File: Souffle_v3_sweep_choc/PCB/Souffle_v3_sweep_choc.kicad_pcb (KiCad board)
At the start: 2 copper layers, 132.1 x 108 mm, 84 parts, among them J1 LED, J2 4PIN, J3 OLED, J4 Conn_01x01_Female, J5 Conn_01x01_Female, SW1 SW_PUSH, SW10 SW_PUSH, SW11 SW_PUSH, SW12 SW_PUSH, SW13 SW_PUSH, SW14 SW_PUSH, SW15 SW_PUSH, SW16 SW_PUSH, SW17 SW_PUSH, SW18 SW_PUSH, SW19 SW_PUSH, SW2 SW_PUSH, SW20 SW_PUSH, SW21 SW_PUSH, SW22 SW_PUSH, SW23 SW_PUSH, SW24 SW_PUSH, SW25 SW_PUSH, SW25b1 RotaryEncoder_Switch, SW26 SW_PUSH, SW27 SW_PUSH, SW28 SW_PUSH, SW29 SW_PUSH, SW3 SW_PUSH, SW30 SW_PUSH, SW31 SW_SPDT, SW4 SW_PUSH, SW5 SW_PUSH, SW6 SW_PUSH, SW7 SW_PUSH, SW8 SW_PUSH, SW9 SW_PUSH, U1 ProMicro

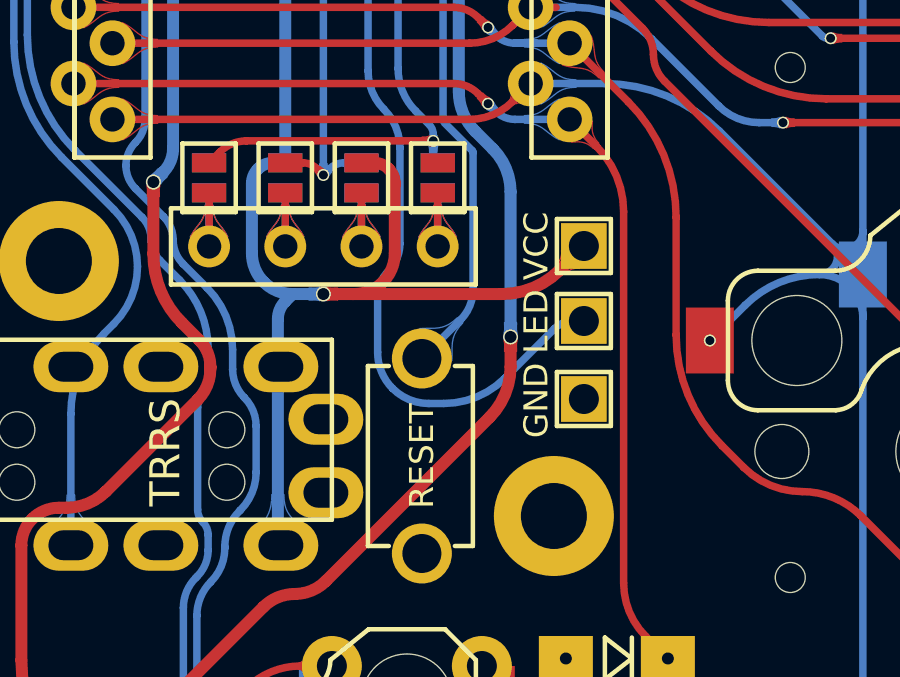
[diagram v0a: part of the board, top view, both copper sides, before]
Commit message: Fixed small bug, completed comment layer.
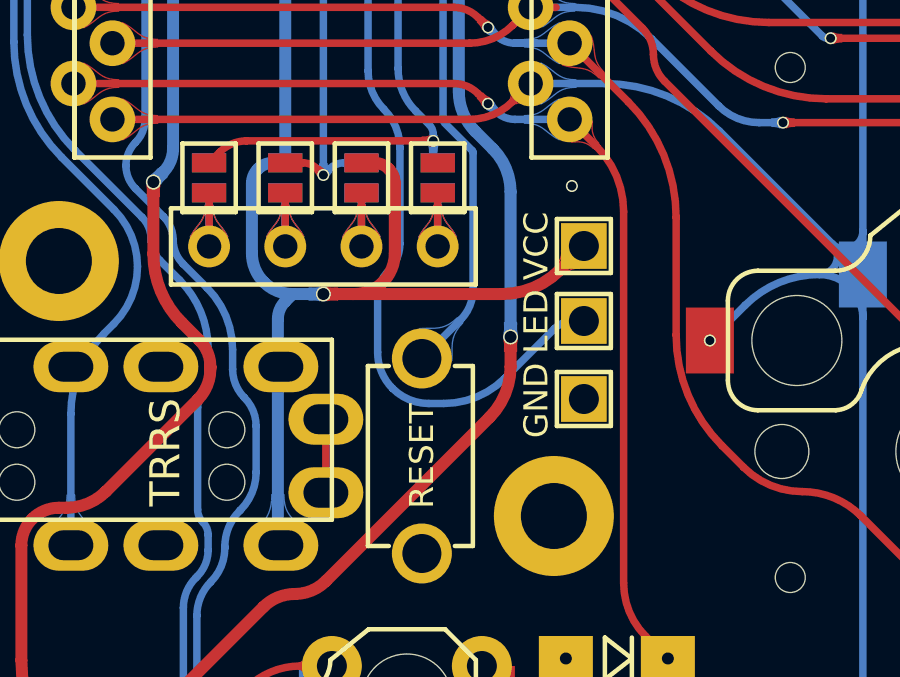
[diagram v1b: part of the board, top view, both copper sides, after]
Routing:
- net unconnected-(J2-Pad4): track 0.00 -> 2.45 mm
- net GND: vias 0 -> 1

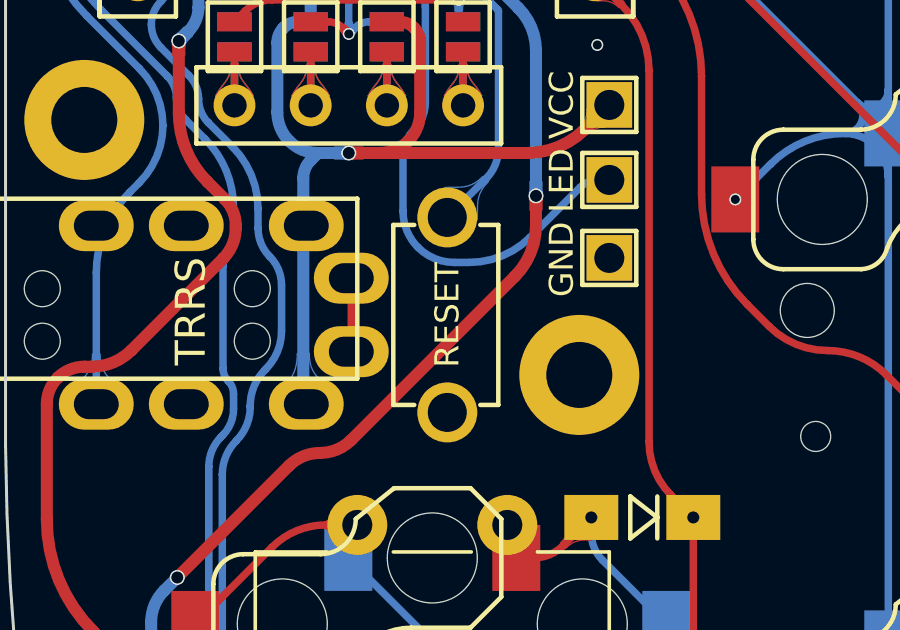
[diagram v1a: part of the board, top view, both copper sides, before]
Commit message: Push reset button away from the TRRS conenctor.
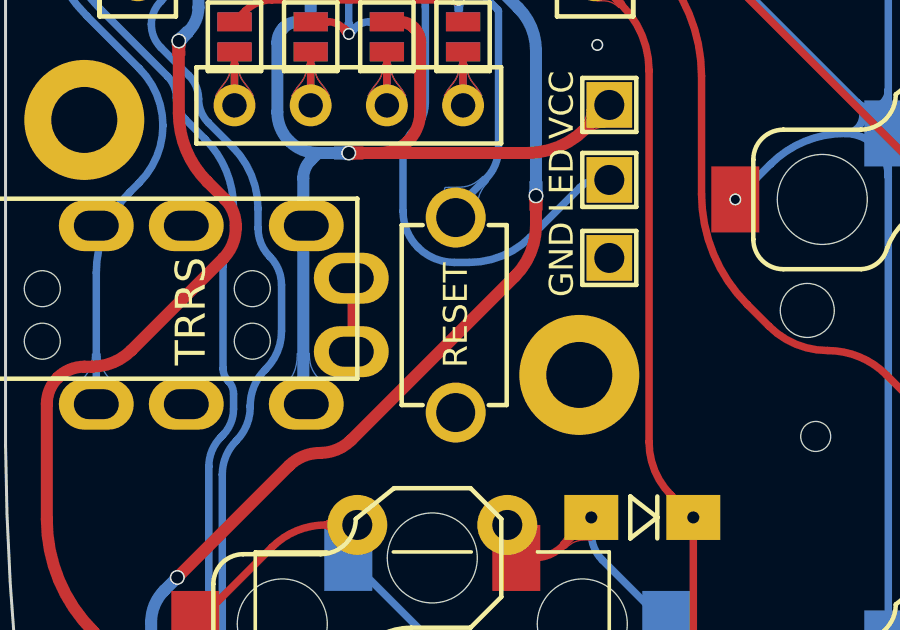
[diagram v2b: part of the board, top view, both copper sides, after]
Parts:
- moved RSW1 0.28 mm to (88.9, 85.7)
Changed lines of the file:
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@@
   )
   (footprint "SofleKeyboard-footprint:TACT_SWITCH_TVBP06" (layer "F.Cu")
-    (at 88.634 85.723139 90)
+    (at 88.914548 85.727296 90)
     (property "Sheetfile" "Souffle_v3_sweep.kicad_sch")
     (property "Sheetname" "")

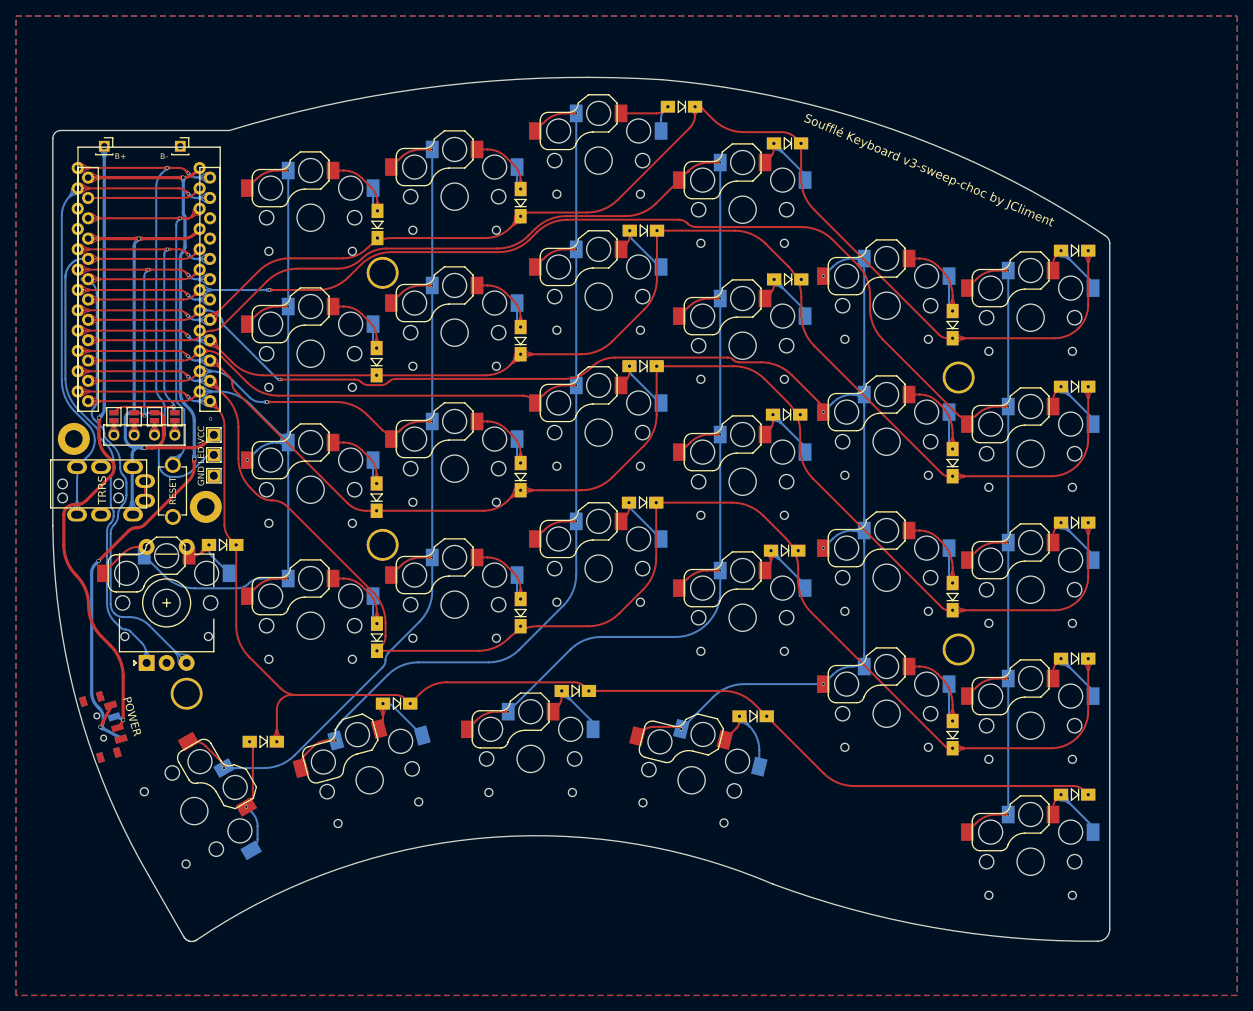
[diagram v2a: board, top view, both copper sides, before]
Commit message: Small changes to make sure the components do not touch each other or the board.
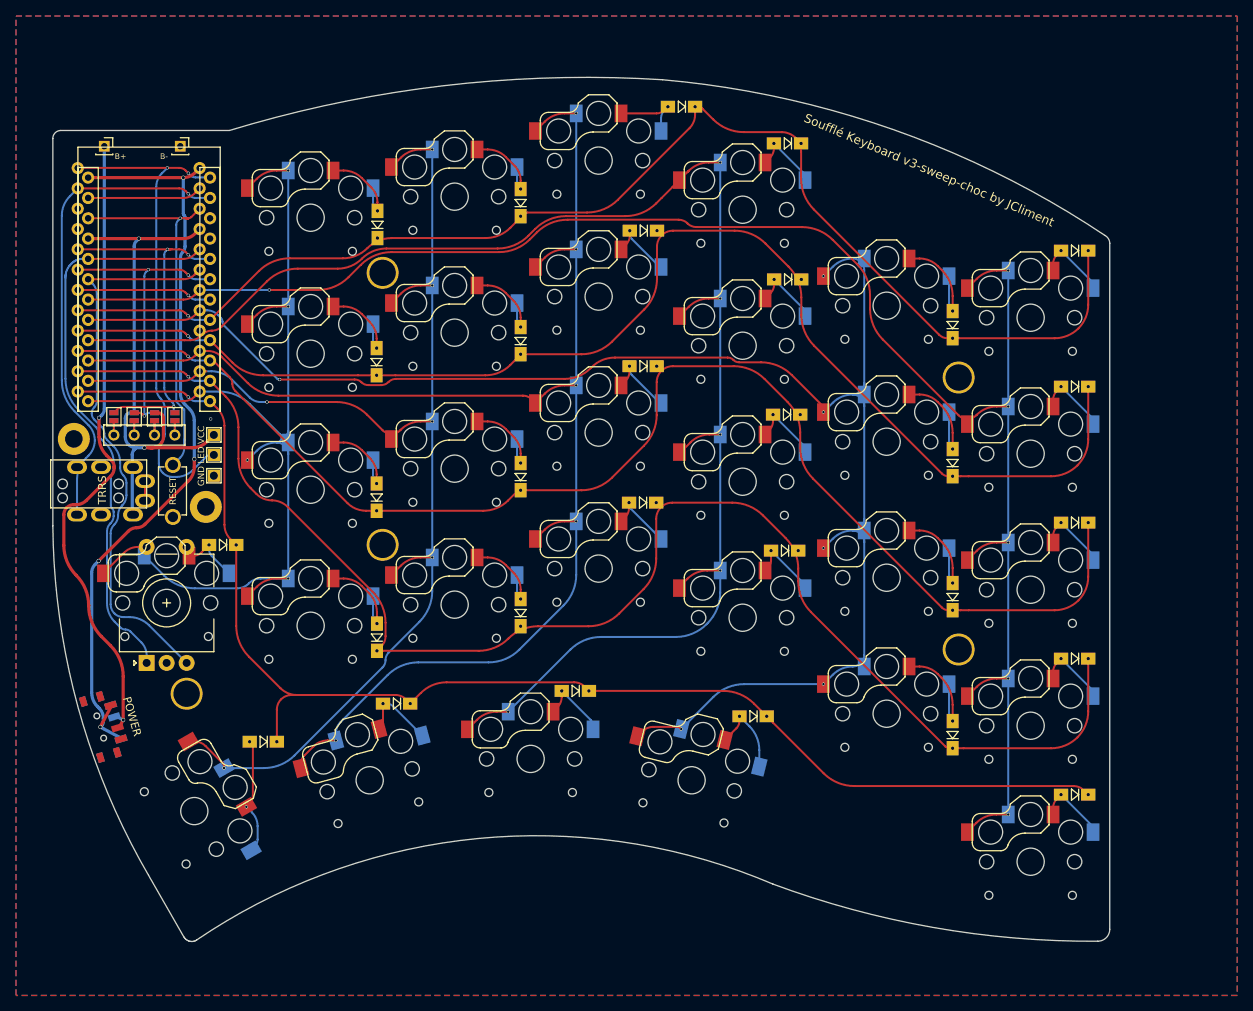
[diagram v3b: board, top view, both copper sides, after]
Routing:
- net row2: track 171.1 -> 170.1 mm
- net row3: track 185.9 -> 185.0 mm
- net row1: track 164.8 -> 163.9 mm
- net row4: track 172.3 -> 173.1 mm
- net RESET: track 46.4 -> 47.1 mm
